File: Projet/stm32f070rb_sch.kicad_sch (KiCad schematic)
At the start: 25 parts

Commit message: board_schematic
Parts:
- C2001: renamed from C?; footprint (none) -> Capacitor_SMD:C_0603_1608Metric_Pad1.08x0.95mm_HandSolder
- JP2001, JP2002, JP2003, JP2004, JP2005, JP2006, JP2007, JP2008: renamed from JP?; footprint (none) -> Jumper:SolderJumper-2_P1.3mm_Open_TrianglePad1.0x1.5mm
- gave numbers to parts that had none: 16
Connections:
- net STLINK_RX: now also JP2010.2 (B); no longer JP2009.1 (A)
- net STLINK_TX: now also JP2009.1 (A); no longer JP2010.2 (B)
- net CLR_FREQ: no longer names the net of U2001.2 (PC12)
- net ESP_STATE: no longer names the net of U2001.22 (PA5)
- no-connect marks 5 -> 29
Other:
- note added: "STM32G070RBT6"

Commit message: pcb_begin
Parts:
- removed SW2001: reset, symbol Switch:SW_Push
- added SW201: SW_MEC_5E, Button_Switch_SMD:SW_SPST_Omron_B3FS-100xP, symbol Switch:SW_MEC_5E
- renumbered C2001 to C201, C2002 to C202, C2003 to C203, C2004 to C204, C2005 to C205, C2006 to C206, D2001 to D201, D2002 to D202, J2001 to J201, JP2001 to JP201, JP2002 to JP202, JP2003 to JP203, JP2004 to JP204, JP2005 to JP205, JP2006 to JP206, JP2007 to JP207, JP2008 to JP208, JP2009 to JP209, JP2010 to JP210, R2001 to R201, R2002 to R202, R2003 to R203, U2001 to U201, Y2001 to Y201
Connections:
- net GND: now also SW201.1, SW201.2
- net STLINK_NRST: now also SW201.3 (K), SW201.4 (A)

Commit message: placement
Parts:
- SW201: footprint Button_Switch_SMD:SW_SPST_Omron_B3FS-100xP -> Button_Switch_SMD:SW_SPST_EVQQ2
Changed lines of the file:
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@@
 (kicad_sch (version 20211123) (generator eeschema)
   (paper "A4")
-  (junction (at 18.796 33.782) (diameter 0) (color 0 0 0 0)
-  )
   (junction (at 234.95 46.99) (diameter 0) (color 0 0 0 0)
   )
@@
   (junction (at 137.16 100.33) (diameter 0) (color 0 0 0 0)
   )
+  (junction (at 18.796 31.75) (diameter 0) (color 0 0 0 0)
+  )
   (junction (at 137.16 115.57) (diameter 0) (color 0 0 0 0)
   )
+  (junction (at 21.336 31.75) (diameter 0) (color 0 0 0 0)
+  )
   (junction (at 165.1 115.57) (diameter 0) (color 0 0 0 0)
-  )
-  (junction (at 18.796 31.75) (diameter 0) (color 0 0 0 0)
   )
   (junction (at 18.796 43.942) (diameter 0) (color 0 0 0 0)
@@
     (stroke (width 0) (type default) (color 0 0 0 0))
   )
-  (wire (pts (xy 18.796 31.75) (xy 27.94 31.75))
-    (stroke (width 0) (type default) (color 0 0 0 0))
-  )
   (wire (pts (xy 38.1 116.84) (xy 50.8 116.84))
     (stroke (width 0) (type default) (color 0 0 0 0))
@@
     (stroke (width 0) (type default) (color 0 0 0 0))
   )
+  (wire (pts (xy 21.336 31.75) (xy 21.336 33.782))
+    (stroke (width 0) (type default) (color 0 0 0 0))
+  )
   (wire (pts (xy 133.35 101.6) (xy 133.35 100.33))
     (stroke (width 0) (type default) (color 0 0 0 0))
@@
     (stroke (width 0) (type default) (color 0 0 0 0))
   )
+  (wire (pts (xy 21.336 31.75) (xy 27.94 31.75))
+    (stroke (width 0) (type default) (color 0 0 0 0))
+  )
   (wire (pts (xy 257.81 46.99) (xy 246.38 46.99))
     (stroke (width 0) (type default) (color 0 0 0 0))
@@
     (stroke (width 0) (type default) (color 0 0 0 0))
   )
+  (wire (pts (xy 18.796 33.782) (xy 18.796 31.75))
+    (stroke (width 0) (type default) (color 0 0 0 0))
+  )
   (wire (pts (xy 90.17 171.45) (xy 90.17 176.53))
     (stroke (width 0) (type default) (color 0 0 0 0))
@@
     (stroke (width 0) (type default) (color 0 0 0 0))
   )
-  (wire (pts (xy 18.796 31.75) (xy 18.796 33.782))
+  (wire (pts (xy 18.796 31.75) (xy 21.336 31.75))
     (stroke (width 0) (type default) (color 0 0 0 0))
   )
@@
   )
   (wire (pts (xy 133.35 100.33) (xy 137.16 100.33))
-    (stroke (width 0) (type default) (color 0 0 0 0))
-  )
-  (wire (pts (xy 18.796 33.782) (xy 21.336 33.782))
     (stroke (width 0) (type default) (color 0 0 0 0))
   )
@@
       (effects (font (size 1.27 1.27)) (justify right))
     )
-    (property "Footprint" "Button_Switch_SMD:SW_SPST_Omron_B3FS-100xP" (id 2) (at 13.716 38.862 0)
-      (effects (font (size 1.27 1.27)) hide)
-    )
+    (property "Footprint" "Button_Switch_SMD:SW_SPST_EVQQ2" (id 2) (at 13.716 38.862 0)
+      (effects (font (size 1.27 1.27)) hide)
+    )

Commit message: Routing
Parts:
- removed SW201: SW_MEC_5E, Button_Switch_SMD:SW_SPST_EVQQ2, symbol Switch:SW_MEC_5E
- added S201: 2-1437565-7, 2-1437565-7 (1):SW_2-1437565-7, symbol 2-1437565-7:2-1437565-7
- J201: footprint Connector_PinHeader_1.00mm:PinHeader_2x07_P1.00mm_Vertical -> Connector_PinHeader_1.27mm:PinHeader_2x07_P1.27mm_Vertical_SMD
- R201, R202: value 60R -> 1k
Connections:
- net +3.3V: now also U201.7 (VREF+)
- net BAT_LED: no longer U201.58 (PB4)
- net GND: now also S201.3, S201.4
- net STLINK_NRST: now also S201.2; no longer C201.1, U201.12 (~{NRST})
- new net: C201.1, S201.1, U201.12 (~{NRST})
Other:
- note added: "first 100 nF for Vref (ADC) second 100 nF for VDD"
- note removed: "R=(VCC-Vled)/Iled =60R Iled=20mA Vled=2.1V"
- moved on the sheet: C201, R202

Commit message: PCB_ROUTAGE
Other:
- moved on the sheet: C202, R201, R202
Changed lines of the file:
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@@
     (stroke (width 0) (type default) (color 0 0 0 0))
   )
-  (wire (pts (xy 76.2 176.53) (xy 76.2 180.34))
+  (wire (pts (xy 76.2 177.8) (xy 76.2 180.34))
     (stroke (width 0) (type default) (color 0 0 0 0))
   )
@@
     (stroke (width 0) (type default) (color 0 0 0 0))
   )
-  (wire (pts (xy 90.17 179.07) (xy 90.17 184.658))
-    (stroke (width 0) (type default) (color 0 0 0 0))
-  )
-  (wire (pts (xy 76.2 166.37) (xy 76.2 171.45))
+  (wire (pts (xy 90.17 177.8) (xy 90.17 184.658))
+    (stroke (width 0) (type default) (color 0 0 0 0))
+  )
+  (wire (pts (xy 76.2 166.37) (xy 76.2 172.72))
     (stroke (width 0) (type default) (color 0 0 0 0))
   )
@@
     (stroke (width 0) (type default) (color 0 0 0 0))
   )
-  (wire (pts (xy 90.17 171.45) (xy 90.17 173.99))
+  (wire (pts (xy 90.17 171.45) (xy 90.17 172.72))
     (stroke (width 0) (type default) (color 0 0 0 0))
   )
@@
     (stroke (width 0) (type default) (color 0 0 0 0))
   )
+  (wire (pts (xy 90.17 157.988) (xy 90.17 166.37))
+    (stroke (width 0) (type default) (color 0 0 0 0))
+  )
   (wire (pts (xy 38.354 60.96) (xy 47.752 60.96))
     (stroke (width 0) (type default) (color 0 0 0 0))
@@
     (stroke (width 0) (type default) (color 0 0 0 0))
   )
-  (wire (pts (xy 153.67 115.57) (xy 165.1 115.57))
+  (wire (pts (xy 155.448 115.57) (xy 165.1 115.57))
     (stroke (width 0) (type default) (color 0 0 0 0))
   )
@@
     (stroke (width 0) (type default) (color 0 0 0 0))
   )
-  (wire (pts (xy 148.59 115.57) (xy 137.16 115.57))
+  (wire (pts (xy 150.368 115.57) (xy 137.16 115.57))
     (stroke (width 0) (type default) (color 0 0 0 0))
   )
@@
     )
   )
-  (global_label "BAT_LED" (shape input) (at 90.17 166.37 90) (fields_autoplaced)
-    (effects (font (size 1.27 1.27)) (justify left))
-    (property "Intersheet References" "${INTERSHEET_REFS}" (id 0) (at 90.0906 156.2159 90)
+  (global_label "BAT_LED" (shape input) (at 90.17 157.988 90) (fields_autoplaced)
+    (effects (font (size 1.27 1.27)) (justify left))
+    (property "Intersheet References" "${INTERSHEET_REFS}" (id 0) (at 90.0906 147.8339 90)
       (effects (font (size 1.27 1.27)) (justify left) hide)
     )
@@
     (pin "2")
   )
-  (symbol (lib_id "Device:R_Small") (at 90.17 176.53 180) (unit 1)
-    (in_bom yes) (on_board yes) (fields_autoplaced)
-    (property "Reference" "R202" (id 0) (at 92.71 175.2599 0)
-      (effects (font (size 1.27 1.27)) (justify right))
-    )
-    (property "Value" "1k" (id 1) (at 92.71 177.7999 0)
-      (effects (font (size 1.27 1.27)) (justify right))
-    )
-    (property "Footprint" "Resistor_SMD:R_0603_1608Metric_Pad0.98x0.95mm_HandSolder" (id 2) (at 90.17 176.53 0)
-      (effects (font (size 1.27 1.27)) hide)
-    )
-    (property "Datasheet" "~" (id 3) (at 90.17 176.53 0)
+  (symbol (lib_id "Device:R_Small") (at 90.17 175.26 180) (unit 1)
+    (in_bom yes) (on_board yes) (fields_autoplaced)
+    (property "Reference" "R202" (id 0) (at 92.71 173.9899 0)
+      (effects (font (size 1.27 1.27)) (justify right))
+    )
+    (property "Value" "1k" (id 1) (at 92.71 176.5299 0)
+      (effects (font (size 1.27 1.27)) (justify right))
+    )
+    (property "Footprint" "Resistor_SMD:R_0603_1608Metric_Pad0.98x0.95mm_HandSolder" (id 2) (at 90.17 175.26 0)
+      (effects (font (size 1.27 1.27)) hide)
+    )
+    (property "Datasheet" "~" (id 3) (at 90.17 175.26 0)
       (effects (font (size 1.27 1.27)) hide)
     )
@@
     (pin "1")
   )
-  (symbol (lib_id "Device:C_Small") (at 151.13 115.57 90) (unit 1)
-    (in_bom yes) (on_board yes) (fields_autoplaced)
-    (property "Reference" "C202" (id 0) (at 151.1363 109.22 90))
-    (property "Value" "10pF" (id 1) (at 151.1363 111.76 90))
-    (property "Footprint" "Capacitor_SMD:C_0603_1608Metric_Pad1.08x0.95mm_HandSolder" (id 2) (at 151.13 115.57 0)
-      (effects (font (size 1.27 1.27)) hide)
-    )
-    (property "Datasheet" "~" (id 3) (at 151.13 115.57 0)
+  (symbol (lib_id "Device:C_Small") (at 152.908 115.57 90) (unit 1)
+    (in_bom yes) (on_board yes) (fields_autoplaced)
+    (property "Reference" "C202" (id 0) (at 152.9143 109.22 90))
+    (property "Value" "10pF" (id 1) (at 152.9143 111.76 90))
+    (property "Footprint" "Capacitor_SMD:C_0603_1608Metric_Pad1.08x0.95mm_HandSolder" (id 2) (at 152.908 115.57 0)
+      (effects (font (size 1.27 1.27)) hide)
+    )
+    (property "Datasheet" "~" (id 3) (at 152.908 115.57 0)
       (effects (font (size 1.27 1.27)) hide)
     )
@@
     (pin "2")
   )
-  (symbol (lib_id "Device:R_Small") (at 76.2 173.99 180) (unit 1)
-    (in_bom yes) (on_board yes) (fields_autoplaced)
-    (property "Reference" "R201" (id 0) (at 78.74 172.7199 0)
-      (effects (font (size 1.27 1.27)) (justify right))
-    )
-    (property "Value" "1k" (id 1) (at 78.74 175.2599 0)
-      (effects (font (size 1.27 1.27)) (justify right))
-    )
-    (property "Footprint" "Resistor_SMD:R_0603_1608Metric_Pad0.98x0.95mm_HandSolder" (id 2) (at 76.2 173.99 0)
-      (effects (font (size 1.27 1.27)) hide)
-    )
-    (property "Datasheet" "~" (id 3) (at 76.2 173.99 0)
-      (effects (font (size 1.27 1.27)) hide)
-    )
+  (symbol (lib_id "Device:R_Small") (at 76.2 175.26 180) (unit 1)
+    (in_bom yes) (on_board yes) (fields_autoplaced)
+    (property "Reference" "R201" (id 0) (at 78.74 173.9899 0)
+      (effects (font (size 1.27 1.27)) (justify right))
+    )
+    (property "Value" "1k" (id 1) (at 78.74 176.5299 0)
+      (effects (font (size 1.27 1.27)) (justify right))
+    )
+    (property "Footprint" "Resistor_SMD:R_0603_1608Metric_Pad0.98x0.95mm_HandSolder" (id 2) (at 76.2 175.26 0)
+      (effects (font (size 1.27 1.27)) hide)
+    )
+    (property "Datasheet" "~" (id 3) (at 76.2 175.26 0)
+      (effects (font (size 1.27 1.27)) hide)
+    )

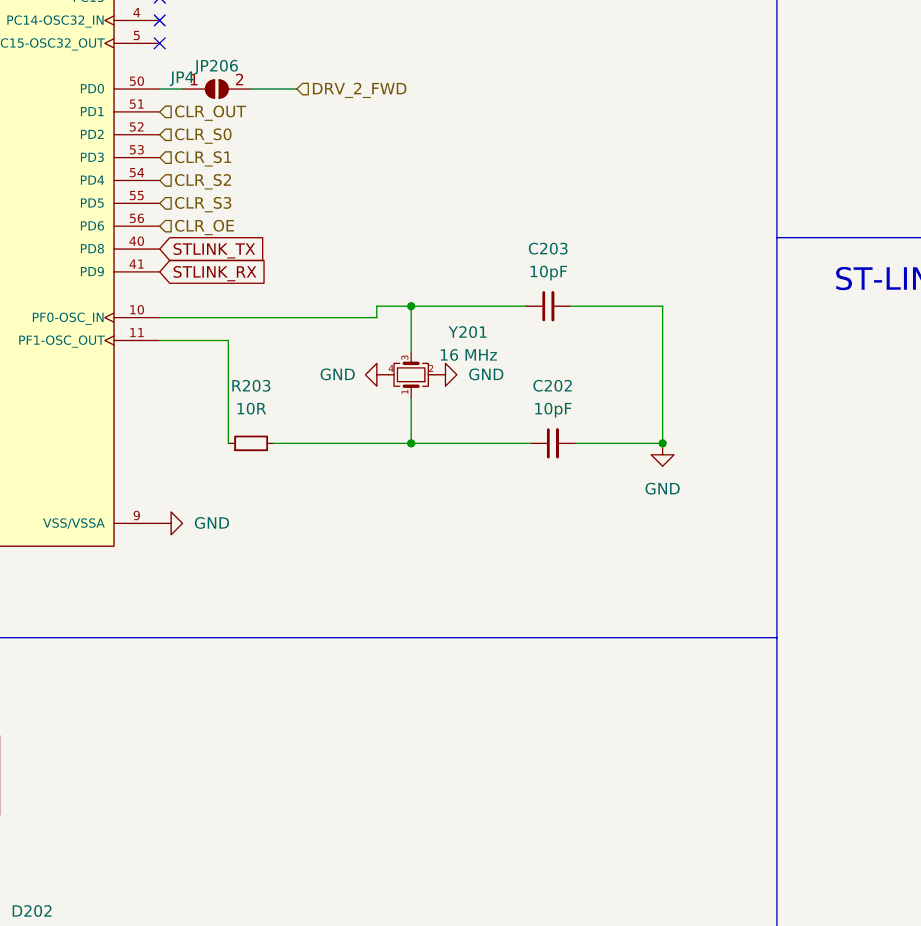
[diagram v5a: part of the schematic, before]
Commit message: PCB_ROUTAGE_Modif
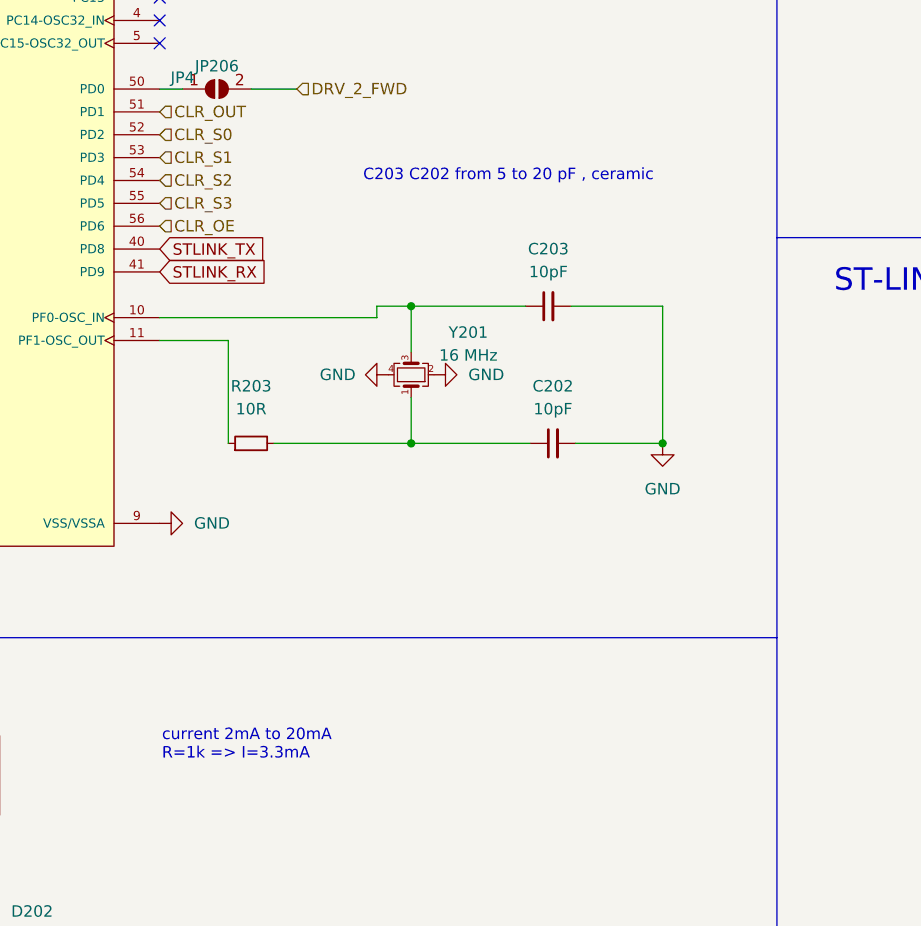
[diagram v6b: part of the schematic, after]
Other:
- note added: "C203 C202 from 5 to 20 pF , ceramic"
- note added: "current 2mA to 20mA R=1k => I=3.3mA"
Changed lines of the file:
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@@
     (effects (font (size 2.5 2.5)) (justify left bottom))
+  )
+  (text "current 2mA to 20mA \nR=1k => I=3.3mA" (at 109.474 150.876 0)
+    (effects (font (size 1.27 1.27)) (justify left bottom))
+  )
+  (text "C203 C202 from 5 to 20 pF , ceramic " (at 131.826 86.614 0)
+    (effects (font (size 1.27 1.27)) (justify left bottom))
   )
   (global_label "STLINK_NRST" (shape input) (at 243.84 133.35 0) (fields_autoplaced)

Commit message: Routage_fini
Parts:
- removed JP201, JP202, JP207, JP208: JP3, Jumper:SolderJumper-2_P1.3mm_Open_TrianglePad1.0x1.5mm, symbol Jumper:SolderJumper_2_Open
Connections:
- net ENC_1_A: now also U201.36 (PA8)
- net ENC_1_B: now also U201.37 (PA9)
- net ENC_2_A: now also U201.38 (PC6)
- net ENC_2_B: now also U201.39 (PC7)
- net OPTQ1: now also U201.14 (PC1); no longer U201.48 (PC8)
- net OPTQ2: now also U201.24 (PA7); no longer U201.47 (PA15)
- net TOF2_GPIO1: now also U201.48 (PC8); no longer U201.28 (PB1)
- net TOF2_XSHUT: now also U201.47 (PA15); no longer U201.29 (PB2)
- net DRV_2_FWD_JP: now reaches JP206.1 (A), U201.50 (PD0)
- net ST_LINK_TX: now reaches J201.13 (Pin_13), JP209.2 (B)
- net NRST_sw: now reaches C201.1, S201.1, U201.12 (~{NRST})
- net ST_LINK_RX: now reaches J201.14 (Pin_14), JP210.1 (A)
- net LED_line: now reaches D201.1 (K), R201.2
- net DRV_2_REV_JP: now reaches JP203.2 (B), U201.60 (PB6)
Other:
- moved on the sheet: JP203, JP206, JP209, JP210

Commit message: Routage_Final
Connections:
- net CLR_LED: now reaches U201.58 (PB4)
- no-connect marks 29 -> 28
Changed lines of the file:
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@@
   (no_connect (at 58.42 63.5))
   (no_connect (at 58.42 53.34))
-  (no_connect (at 58.42 91.44))
   (wire (pts (xy 32.512 96.52) (xy 34.29 96.52))
     (stroke (width 0) (type default) (color 0 0 0 0))
@@
     )
   )
+  (hierarchical_label "CLR_LED" (shape input) (at 58.42 91.44 180)
+    (effects (font (size 1.27 1.27)) (justify right))
+  )
   (hierarchical_label "CLR_OUT" (shape input) (at 109.22 78.74 0)
